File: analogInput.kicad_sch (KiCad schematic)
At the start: 2 parts, among them J2 AudioJack2, K1 SANYOU_SRD_Form_C

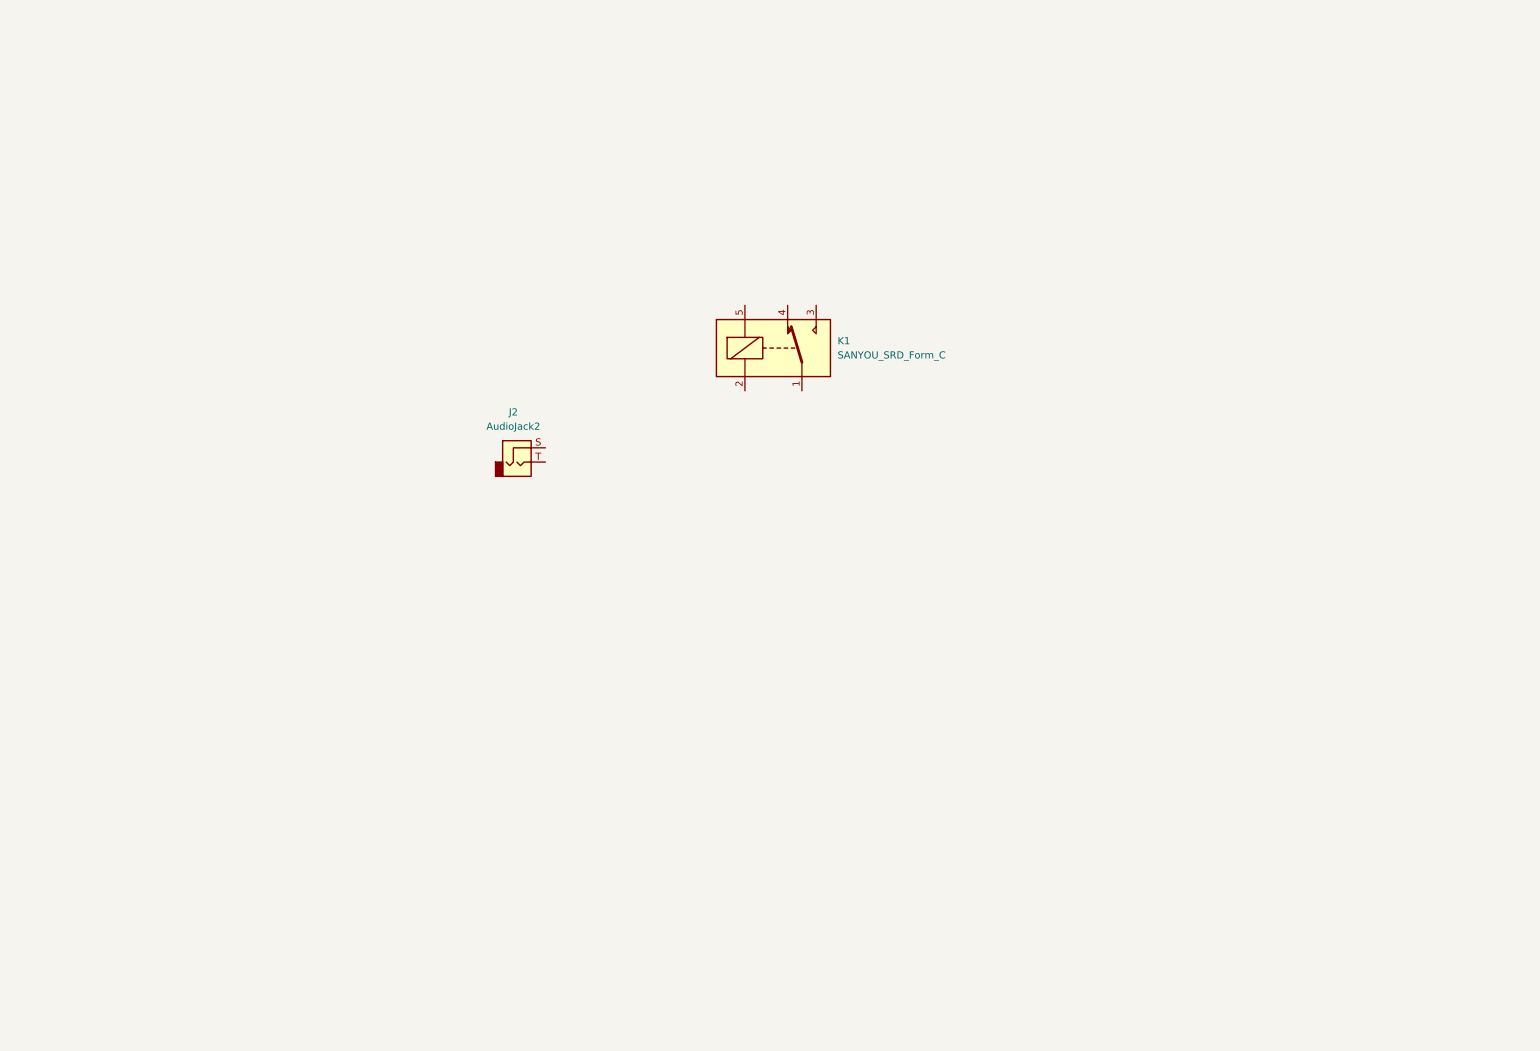
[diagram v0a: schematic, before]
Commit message: feat: Adds MIDI Input
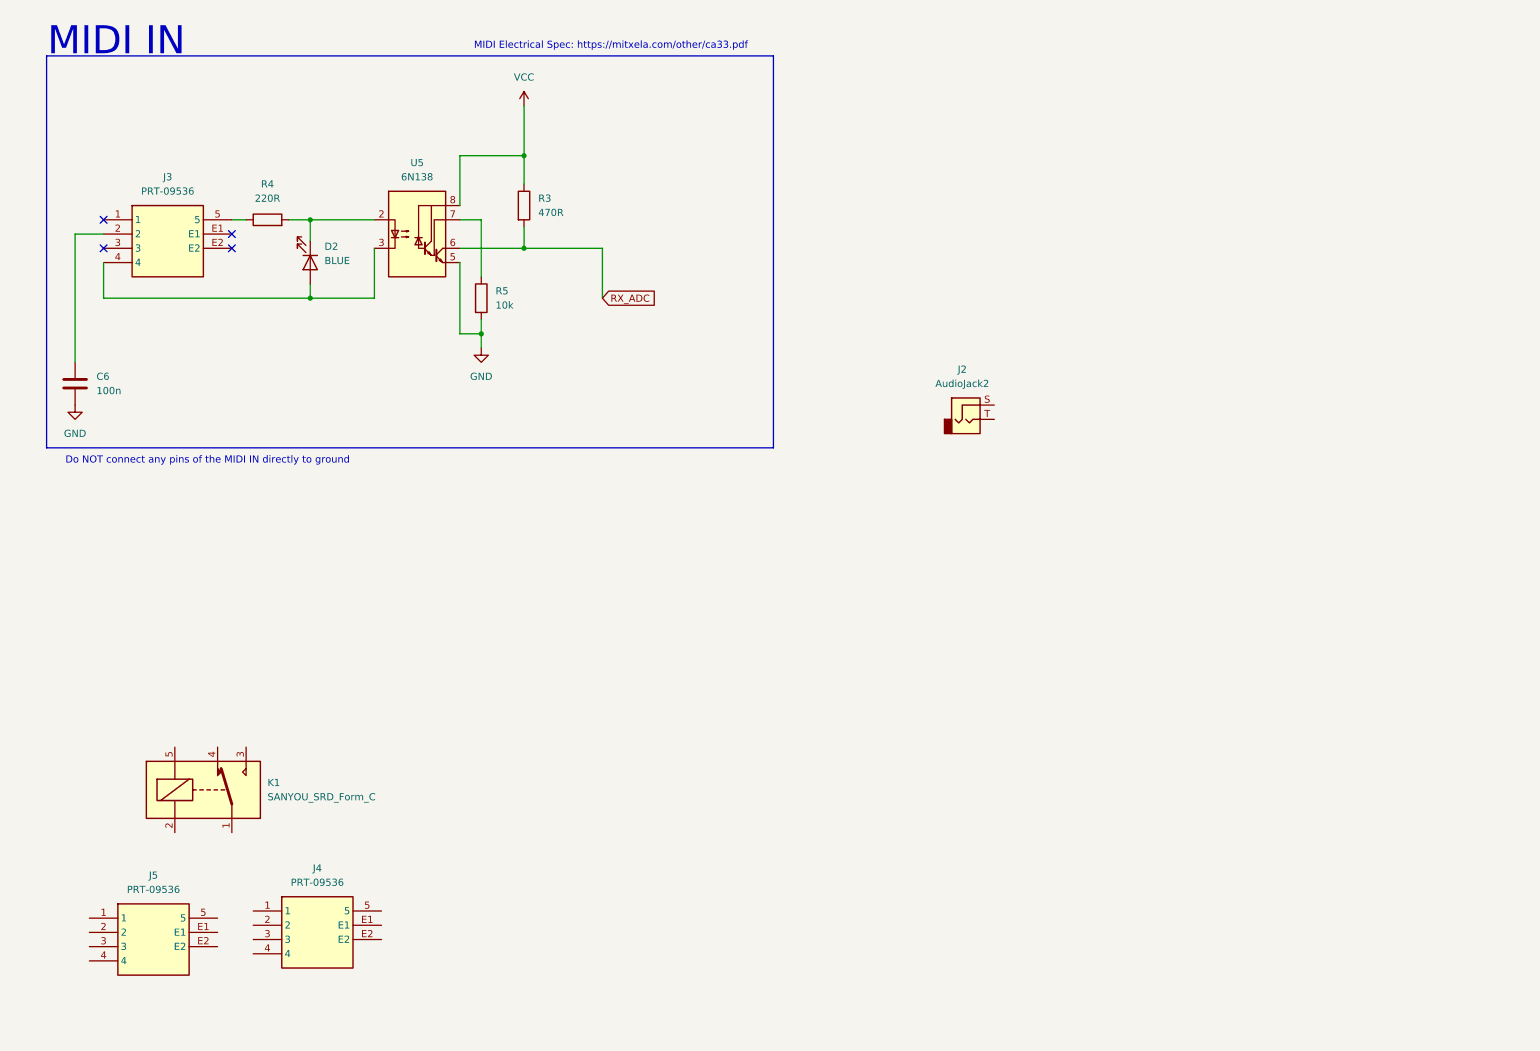
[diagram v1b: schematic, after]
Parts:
- added C6: 100n, symbol Device:C
- added D2: BLUE, symbol Device:LED
- added J3, J4, J5: PRT-09536, PRT09536, symbol PRT-09536:PRT-09536
- added R3: 470R, symbol Device:R
- added R4: 220R, symbol Device:R
- added R5: 10k, symbol Device:R
- added U5: 6N138, symbol Isolator:6N138
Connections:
- new net: D2.1 (K), R4.2, U5.2 (C1)
- new net: D2.2 (A), J3.4, U5.3 (C2)
- new net: J3.5, R4.1
- new net: R5.1, U5.7 (VO1)
- new net: C6.1, J3.2
- new net GND: C6.2, R5.2, U5.5 (GND)
- new net RX_ADC: R3.2, U5.6 (VO2)
- new net VCC: R3.1, U5.8 (VCC)
- no-connect marks 0 -> 4
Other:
- note added: "Do NOT connect any pins of the MIDI IN directly to ground"
- note added: "MIDI Electrical Spec: https://mitxela.com/other/ca33.pdf"
- note added: "MIDI IN"
- moved on the sheet: J2, K1

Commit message: feat: Adds Analog input + ADC
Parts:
- removed J2: AudioJack2, symbol Connector_Audio:AudioJack2
- removed J4, J5: PRT-09536, PRT09536, symbol PRT-09536:PRT-09536
- added C10, C12, C7, C8, C9: 10u, symbol Device:C
- added C11: 0.1u, symbol Device:C
- added J2: AudioJack3_Dual_Switch, symbol Connector_Audio:AudioJack3_Dual_Switch
- added R10, R11, R12, R13: 100R, symbol Device:R
- added R14, R15: 700R, symbol Device:R
- added R6, R7, R8, R9: 100k, symbol Device:R
- added U6: MCP3422Axx-xSN, Package_SO:SOIC-8_3.9x4.9mm_P1.27mm, symbol Analog_ADC:MCP3422Axx-xSN
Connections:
- net GND: now also C11.1, C12.1, J2.RN1, J2.RN2, J2.S1, J2.S2, J2.SN1, J2.SN2, J2.TN1, J2.TN2, R6.2, R7.2, R8.2, R9.2, U6.6 (V_{SS})
- net RX_ADC renamed RX
- new net: R11.1, U6.2 (CH1-)
- new net: C8.1, R11.2
- new net: R10.1, U6.1 (CH1+)
- new net: C7.1, R10.2
- new net: R13.1, U6.8 (CH2-)
- new net: C10.1, R13.2
- new net: R12.1, U6.7 (CH2+)
- new net: C9.1, R12.2
- new net +3V3: C11.2, C12.2, U6.3 (V_{DD})
- new net VDD: R14.1, R15.1
- new net inl+: C10.2, J2.T1, R9.1
- new net inl-: C9.2, J2.R1, R8.1
- new net inr+: C7.2, J2.T2, R6.1
- new net inr-: C8.2, J2.R2, R7.1
- new net scl: R14.2, U6.5 (SCL)
- new net sda: R15.2, U6.4 (SDA)
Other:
- note added: "ADC"
- note added: "JACKS"
- note added: "Per Datasheet: Pullups should be in [5k, 10k] for [100kHz, 400kHz] sampling rate ~700R for 3.45MHz sampling rate"
- moved on the sheet: K1
